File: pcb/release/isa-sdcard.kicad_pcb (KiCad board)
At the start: 2 copper layers, 151.6 x 82.7 mm, 47 parts, among them J1 SDCARD, J2 Bus_ISA_8bit_AB_Rev0, SW1 ADDR SEL, U1 74HC00, U10 74HC74, U11 74HC08, U12 74HC04, U13 74HC74, U2 74HCT32, U3 74HCT139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

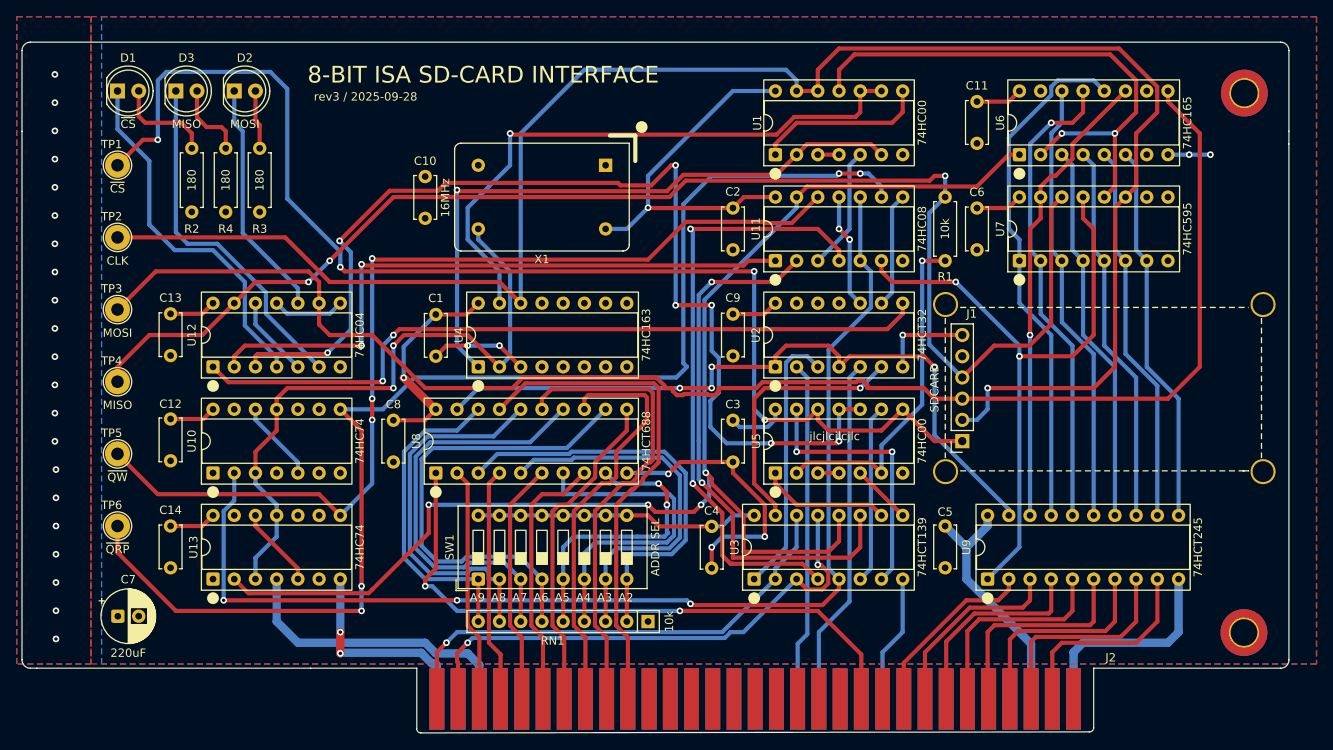
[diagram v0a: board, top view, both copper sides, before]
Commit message: Adding PCB variant
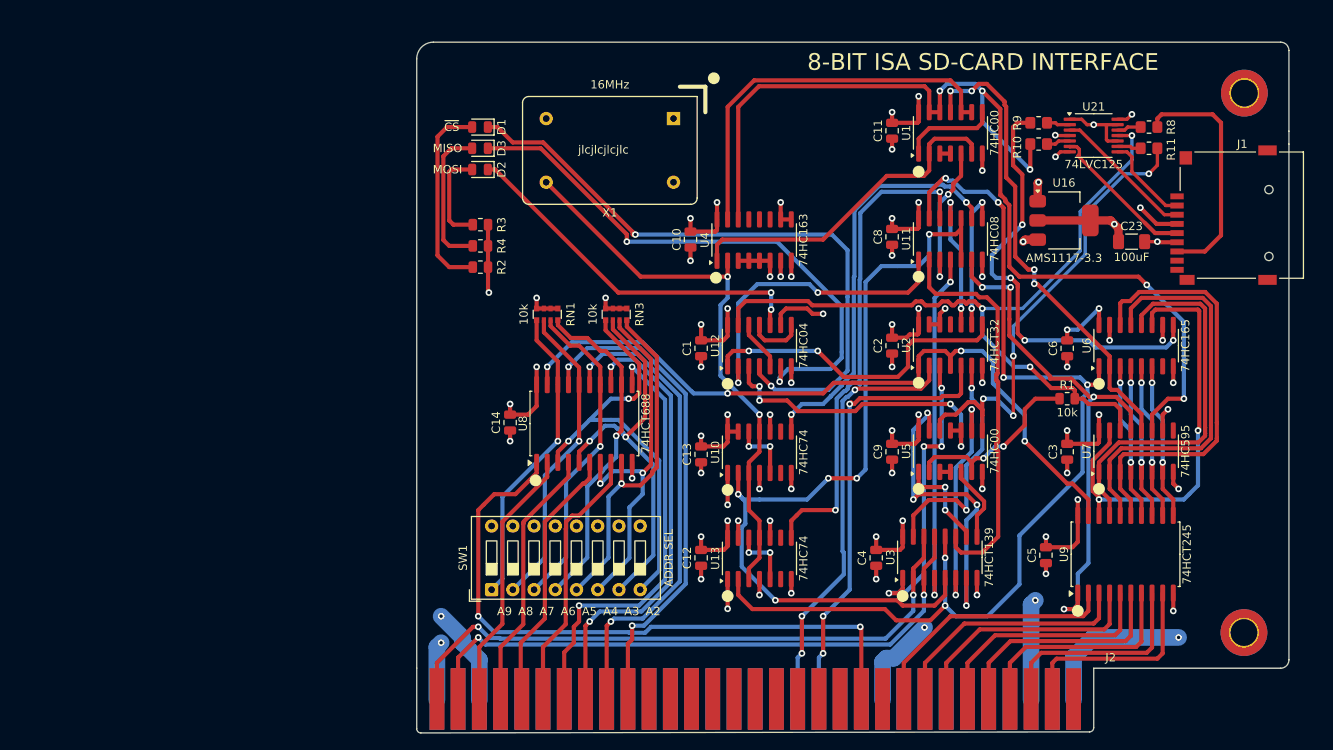
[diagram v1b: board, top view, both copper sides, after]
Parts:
- removed C7: 220uF, Capacitor_THT:CP_Radial_D6.3mm_P2.50mm
- removed TP1: ~{CS}, TestPoint:TestPoint_Loop_D2.54mm_Drill1.5mm_Beaded
- removed TP2: CLK, TestPoint:TestPoint_Loop_D2.54mm_Drill1.5mm_Beaded
- removed TP3: MOSI, TestPoint:TestPoint_Loop_D2.54mm_Drill1.5mm_Beaded
- removed TP4: MISO, TestPoint:TestPoint_Loop_D2.54mm_Drill1.5mm_Beaded
- removed TP5: ~{QW}, TestPoint:TestPoint_Loop_D2.54mm_Drill1.5mm_Beaded
- removed TP6: ~{QRP}, TestPoint:TestPoint_Loop_D2.54mm_Drill1.5mm_Beaded
- added C23: 100uF, Capacitor_SMD:C_1206_3216Metric_Pad1.33x1.80mm_HandSolder, F.Cu at (162.2, 61.5)
- added R10: 3.3k, Resistor_SMD:R_0805_2012Metric_Pad1.20x1.40mm_HandSolder, F.Cu at (151.1, 49.8)
- added R11: 3.3k, Resistor_SMD:R_0805_2012Metric_Pad1.20x1.40mm_HandSolder, F.Cu at (164.3, 50.3)
- added R8: 3.3k, Resistor_SMD:R_0805_2012Metric_Pad1.20x1.40mm_HandSolder, F.Cu at (164.3, 47.7)
- added R9: 3.3k, Resistor_SMD:R_0805_2012Metric_Pad1.20x1.40mm_HandSolder, F.Cu at (151.1, 47.2)
- added RN3: 10k, Resistor_SMD:R_Array_Convex_4x0612, F.Cu at (100.6, 70.2)
- added U16: AMS1117-3.3, Package_TO_SOT_SMD:SOT-223-3_TabPin2, F.Cu at (154.2, 58.9)
- added U21: 74LVC125, Package_SO:TSSOP-14_4.4x5mm_P0.65mm, F.Cu at (157.7, 48.8)
- C1, C10, C11, C12, C13, C14, C2, C3, C4, C5, C6, C8, C9: footprint Capacitor_THT:C_Disc_D5.0mm_W2.5mm_P5.00mm -> Capacitor_SMD:C_0805_2012Metric
- D1, D2, D3: footprint LED_THT:LED_D5.0mm -> LED_SMD:LED_0805_2012Metric
- J1: value SDCARD -> Micro_SD_Card_Det1; footprint sdcard-holder:sdcard-socket -> components:CONN9_MSD-1_CUD
- R1, R2, R3, R4: footprint Resistor_THT:R_Axial_DIN0207_L6.3mm_D2.5mm_P7.62mm_Horizontal -> Resistor_SMD:R_0805_2012Metric
- RN1: footprint Resistor_THT:R_Array_SIP9 -> Resistor_SMD:R_Array_Convex_4x0612
- U1, U10, U11, U12, U13, U2, U5: footprint Package_DIP:DIP-14_W7.62mm_Socket -> Package_SO:SOIC-14_3.9x8.7mm_P1.27mm
- U3, U4, U6, U7: footprint Package_DIP:DIP-16_W7.62mm_Socket -> Package_SO:SOIC-16_3.9x9.9mm_P1.27mm
- U8, U9: footprint Package_DIP:DIP-20_W7.62mm_Socket -> Package_SO:SOIC-20W_7.5x12.8mm_P1.27mm
- moved C8 65.5 mm to (133.6, 60.9)
- moved U12 65.5 mm to (117.7, 73.9)
- moved U10 65.5 mm to (117.7, 86.7)
- moved U13 65.5 mm to (117.7, 99.4)
- moved C13 64.6 mm to (110.7, 86.9)
- moved C12 64.6 mm to (110.7, 99.3)
- moved C14 44.2 mm to (87.9, 83.1)
- moved D1 43.6 mm to (84.3, 47.7), turned to 180 degrees
- moved J1 43.0 mm to (175.4, 58.3), turned to 90 degrees
- moved C3 40.0 mm to (154.5, 86.6)
- moved RN1 38.7 mm to (92.3, 70.2), turned to -90 degrees
- moved R2 37.4 mm to (84.3, 64.5), turned to 0 degrees
- moved D3 37.0 mm to (84.3, 50.3), turned to 180 degrees
- moved U4 36.3 mm to (117.1, 61.3)
- moved R4 32.6 mm to (84.3, 62.0), turned to 0 degrees
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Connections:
- J1 pad 1: ~{CS} -> unconnected-(J1-DAT2-Pad1)
- J1 pad 2: CLK -> CS_LLS
- J1 pad 3: MOSI -> DI_LLS
- J1 pad 4: MISO -> +3V3
- J1 pad 5: VCC -> SCK_LLS
- RN1 pad 2: Net-(RN1-R1) -> GND
- RN1 pad 3: Net-(RN1-R2) -> GND
- RN1 pad 4: Net-(RN1-R3) -> GND
- RN1 pad 5: Net-(RN1-R4) -> Net-(RN1D-R4.2)
- RN1 pad 6: Net-(RN1-R5) -> Net-(RN1C-R3.2)
- RN1 pad 8: Net-(RN1-R7) -> Net-(RN1A-R1.2)
- SW1 pad 1: Net-(RN1-R8) -> Net-(RN1D-R4.2)
- SW1 pad 2: Net-(RN1-R7) -> Net-(RN1C-R3.2)
- SW1 pad 4: Net-(RN1-R5) -> Net-(RN1A-R1.2)
- SW1 pad 5: Net-(RN1-R4) -> Net-(RN3A-R1.2)
- SW1 pad 6: Net-(RN1-R3) -> Net-(RN3B-R2.2)
- SW1 pad 7: Net-(RN1-R2) -> Net-(RN3C-R3.2)
- SW1 pad 8: Net-(RN1-R1) -> Net-(RN3D-R4.2)
- U8 pad 12: Net-(RN1-R5) -> Net-(RN1A-R1.2)
- U8 pad 16: Net-(RN1-R7) -> Net-(RN1C-R3.2)
- U8 pad 18: Net-(RN1-R8) -> Net-(RN1D-R4.2)
- U8 pad 3: Net-(RN1-R1) -> Net-(RN3D-R4.2)
- U8 pad 5: Net-(RN1-R2) -> Net-(RN3C-R3.2)
- U8 pad 7: Net-(RN1-R3) -> Net-(RN3B-R2.2)
- U8 pad 9: Net-(RN1-R4) -> Net-(RN3A-R1.2)
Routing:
- net Net-(U10B-~{Q}): track 150.8 -> 48.9 mm, vias 4 -> 2
- net MOSI: track 180.3 -> 85.2 mm, vias 0 -> 5
- net ~{CS}: track 150.6 -> 57.4 mm
- net CS: track 128.5 -> 37.6 mm, vias 7 -> 4
- net CLK: track 216.5 -> 126.3 mm, vias 1 -> 5
- net MISO: track 165.9 -> 92.5 mm
- net Net-(U13B-~{Q}): track 118.7 -> 59.3 mm, vias 3 -> 2
- net Net-(RN1-R5): track 56.5 -> 0.00 mm
- net Net-(U12-Pad1): track 90.5 -> 38.1 mm
- net Net-(RN3D-R4.2): track 0.00 -> 51.1 mm, vias 0 -> 2
- net Net-(RN1-R1): track 50.5 -> 0.00 mm
- net Net-(RN3C-R3.2): track 0.00 -> 46.7 mm, vias 0 -> 2
- net Net-(RN1-R2): track 45.6 -> 0.00 mm
- net Net-(RN1-R7): track 45.5 -> 0.00 mm
- net Net-(RN3B-R2.2): track 0.00 -> 44.8 mm, vias 0 -> 2
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- added copper zone on In1.Cu, net GND
- added copper zone on In2.Cu, net VCC
- removed copper zone on B.Cu, net GND
- removed copper zone on F.Cu, net GND
- removed copper zone on B.Cu, net VCC
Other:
- board size 151.6 x 82.7 mm -> 104.4 x 82.7 mm
- copper layers 2 -> 4
- board text removed: "rev3 / 2025-09-28"

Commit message: Fixing CS bug in code, adding logos to PCB
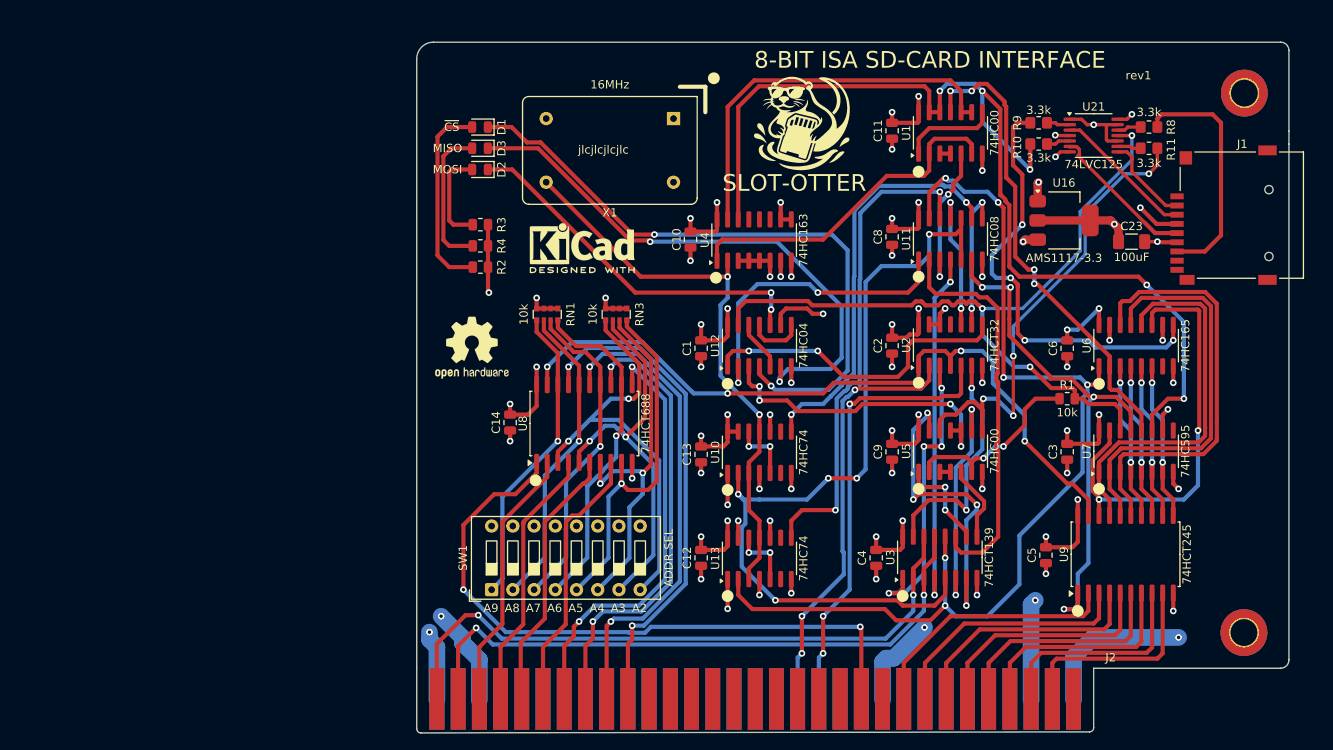
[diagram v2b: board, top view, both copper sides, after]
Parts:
- added G***: LOGO, components:slototter-logo, F.Cu at (122.8, 47.2)
- added REF**: OSHW-Logo2_9.8x8mm_SilkScreen, Symbol:OSHW-Logo2_9.8x8mm_SilkScreen, F.Cu at (83.3, 74.2)
- added REF**: KiCad-Logo2_5mm_SilkScreen, Symbol:KiCad-Logo2_5mm_SilkScreen, F.Cu at (96.5, 62.2)
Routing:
- net A0: track 74.6 -> 77.1 mm
- net A1: track 73.3 -> 75.0 mm
- net GND: track 119.2 -> 120.6 mm
- net Net-(RN3A-R1.2): track 41.9 -> 43.2 mm
- net A6: track 52.8 -> 51.7 mm
- net AEN: track 78.4 -> 79.1 mm
- net Net-(D3-K): track 67.7 -> 67.2 mm
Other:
- board text added: "SLOT-OTTER"
- board text added: "rev1"
